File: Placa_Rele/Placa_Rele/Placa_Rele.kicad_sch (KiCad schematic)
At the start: 43 parts, among them J1 Screw_Terminal_Crusher1, J2 MixerScrewTerminal1, J3 FanScrewTerminal1, Q1 2N3904, Q2 2N3904, Q3 2N3904, U1 LM7805_TO220, U2 ESP32-DEVKIT-V1, U3 PC817, U4 PC817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

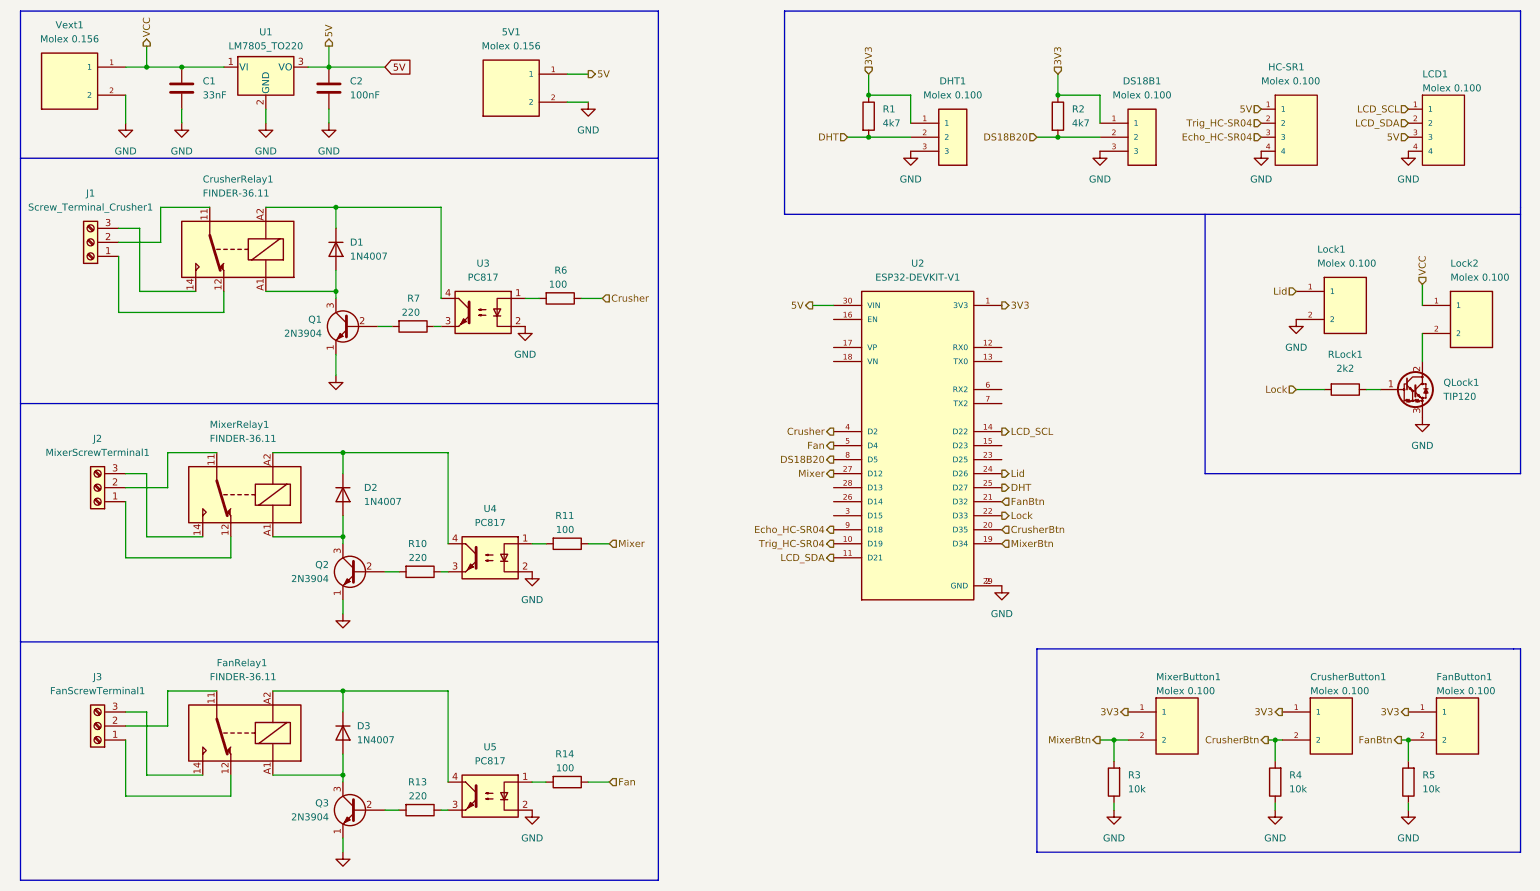
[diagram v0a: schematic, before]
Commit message: Primero Version de PCB con PCB_rele
Primer PCB terminado, los componentes no estan en su posicion final.
El principal problema fue la conexion de 5V, 3v3 y GND en los conectores
del ultrasonico, LCD y DHT.
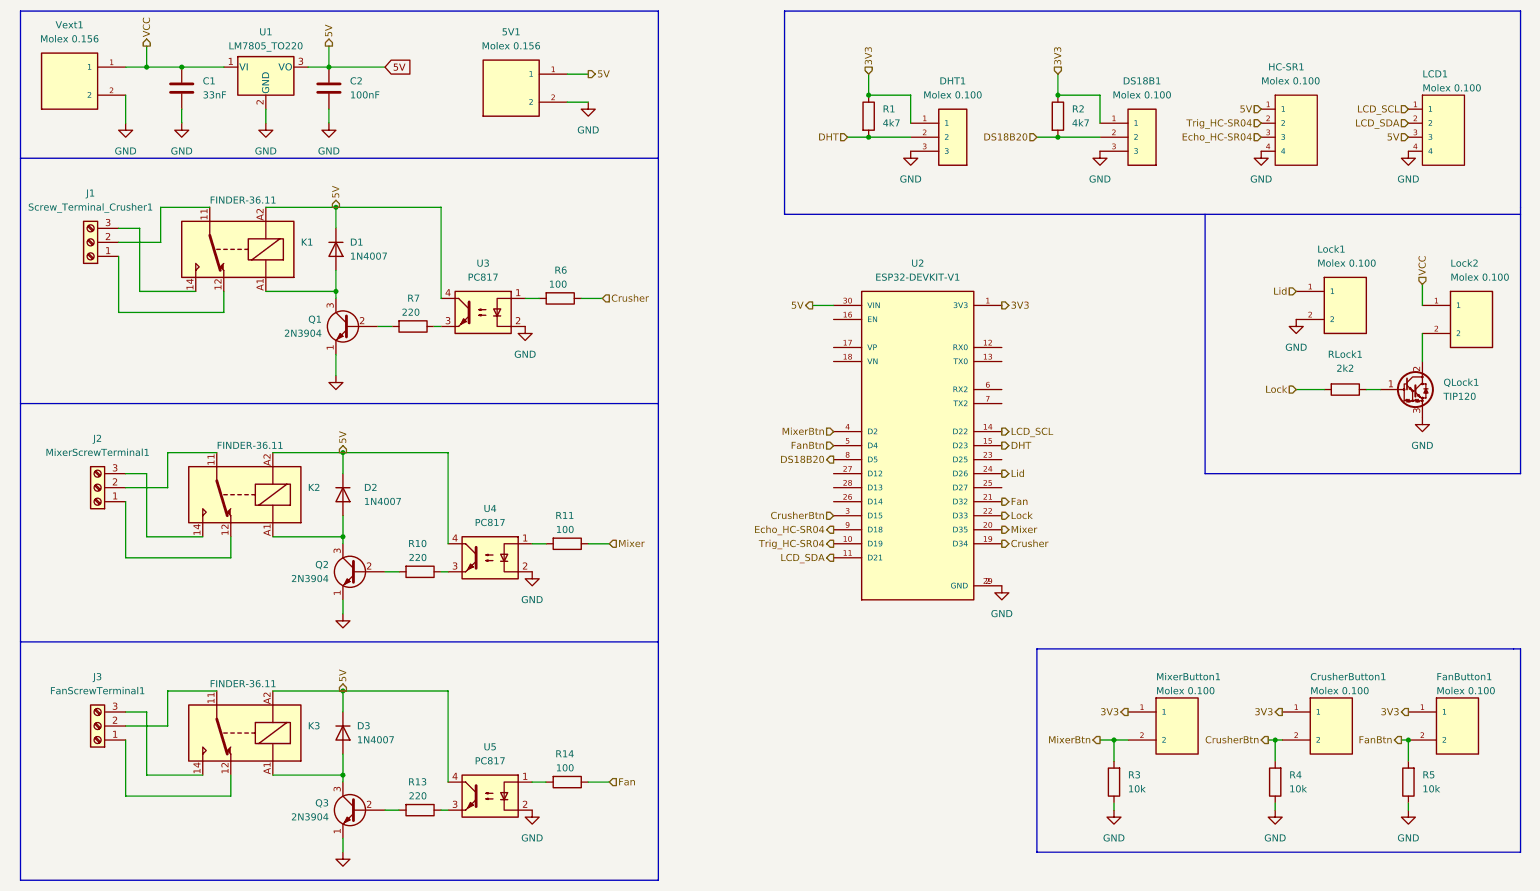
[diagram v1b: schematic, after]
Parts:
- removed CrusherRelay1, FanRelay1, MixerRelay1: FINDER-36.11, Relay_SMD:Relay_DPDT_Kemet_EE2_NU, symbol Relay:FINDER-36.11
- added K1, K2, K3: FINDER-36.11, Relay_THT:Relay_SPDT_Finder_36.11, symbol Relay:FINDER-36.11
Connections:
- net 5V: now also D1.1 (K), D2.1 (K), D3.1 (K), U3.4, U4.4, U5.4, K1.A2, K2.A2, K3.A2
- net Crusher: now also U2.19 (D34); no longer U2.4 (D2)
- net CrusherBtn: now also U2.3 (D15); no longer U2.20 (D35)
- net DHT: now also U2.15 (D23); no longer U2.25 (D27)
- net Fan: now also U2.21 (D32); no longer U2.5 (D4)
- net FanBtn: now also U2.5 (D4); no longer U2.21 (D32)
- net Mixer: now also U2.20 (D35); no longer U2.27 (D12)
- net MixerBtn: now also U2.4 (D2); no longer U2.19 (D34)
- net at J3.2 (Pin_2): now also K3.11
- net at J3.1 (Pin_1): now also K3.12
- net at J3.3 (Pin_3): now also K3.14
- net at D3.2 (A), Q3.3 (C): now also K3.A1
- net at J1.2 (Pin_2): now also K1.11
- net at J1.1 (Pin_1): now also K1.12
- net at J1.3 (Pin_3): now also K1.14
- net at D1.2 (A), Q1.3 (C): now also K1.A1
- net at D2.2 (A), Q2.3 (C): now also K2.A1
- net at J2.2 (Pin_2): now also K2.11
- net at J2.1 (Pin_1): now also K2.12
- net at J2.3 (Pin_3): now also K2.14

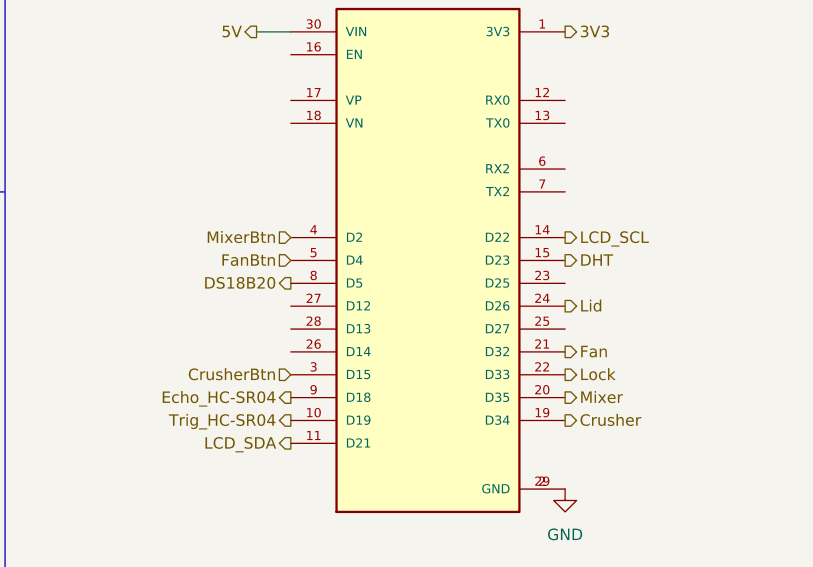
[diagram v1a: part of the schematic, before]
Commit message: Modificacion de PCB
Se cambiaron los ordenes de los GPIO asi DHT y DS18B estaban en los
primeros GPIOS y facilitaba el ruteo.
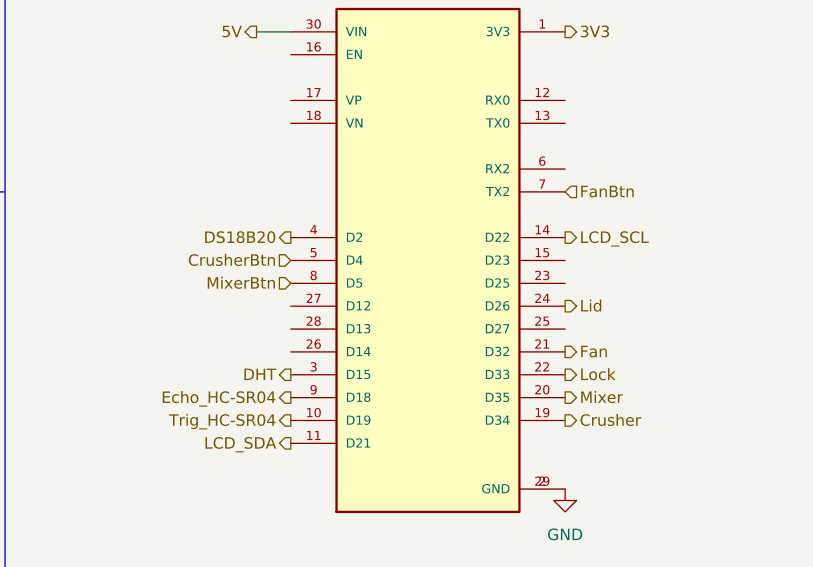
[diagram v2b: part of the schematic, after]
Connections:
- net CrusherBtn: now also U2.5 (D4); no longer U2.3 (D15)
- net DHT: now also U2.3 (D15); no longer U2.15 (D23)
- net DS18B20: now also U2.4 (D2); no longer U2.8 (D5)
- net FanBtn: now also U2.7 (TX2); no longer U2.5 (D4)
- net MixerBtn: now also U2.8 (D5); no longer U2.4 (D2)
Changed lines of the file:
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@@
     (effects (font (size 1.27 1.27)) (justify left))
   )
-  (hierarchical_label "DHT" (shape output) (at 190.5 91.44 0) (fields_autoplaced)
-    (effects (font (size 1.27 1.27)) (justify left))
+  (hierarchical_label "DHT" (shape output) (at 160.02 104.14 180) (fields_autoplaced)
+    (effects (font (size 1.27 1.27)) (justify right))
   )
   (hierarchical_label "Lid" (shape output) (at 190.5 96.52 0) (fields_autoplaced)
@@
     (effects (font (size 1.27 1.27)) (justify right))
   )
-  (hierarchical_label "CrusherBtn" (shape input) (at 160.02 104.14 180) (fields_autoplaced)
+  (hierarchical_label "CrusherBtn" (shape input) (at 160.02 91.44 180) (fields_autoplaced)
     (effects (font (size 1.27 1.27)) (justify right))
   )
@@
     (effects (font (size 1.27 1.27)) (justify right))
   )
-  (hierarchical_label "FanBtn" (shape input) (at 160.02 91.44 180) (fields_autoplaced)
-    (effects (font (size 1.27 1.27)) (justify right))
+  (hierarchical_label "FanBtn" (shape input) (at 190.5 83.82 0) (fields_autoplaced)
+    (effects (font (size 1.27 1.27)) (justify left))
   )
   (hierarchical_label "LCD_SCL" (shape input) (at 264.16 30.48 180) (fields_autoplaced)
@@
     (effects (font (size 1.27 1.27)) (justify left))
   )
-  (hierarchical_label "MixerBtn" (shape input) (at 160.02 88.9 180) (fields_autoplaced)
+  (hierarchical_label "MixerBtn" (shape input) (at 160.02 93.98 180) (fields_autoplaced)
     (effects (font (size 1.27 1.27)) (justify right))
   )
@@
     (effects (font (size 1.27 1.27)) (justify right))
   )
-  (hierarchical_label "DS18B20" (shape output) (at 160.02 93.98 180) (fields_autoplaced)
+  (hierarchical_label "DS18B20" (shape output) (at 160.02 88.9 180) (fields_autoplaced)
     (effects (font (size 1.27 1.27)) (justify right))
   )

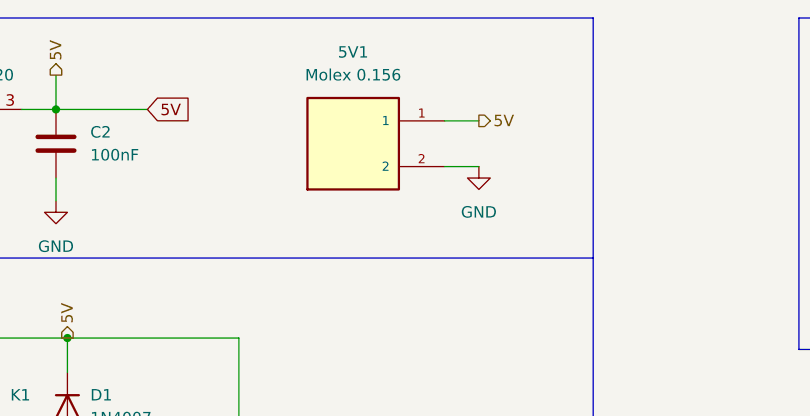
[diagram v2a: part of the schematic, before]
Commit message: Placa final con  reles pero sin LEDS
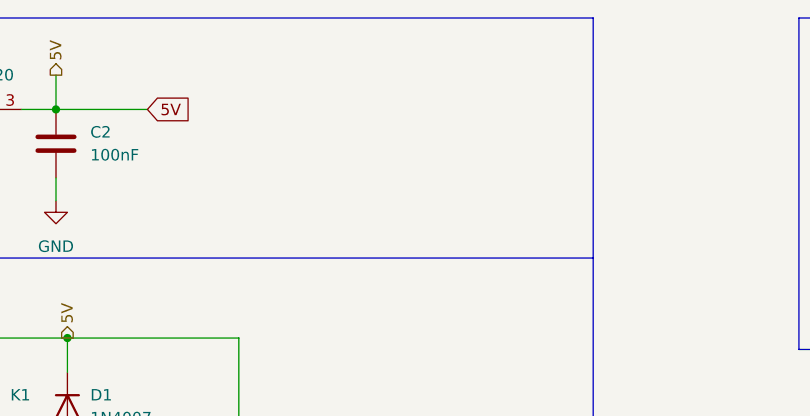
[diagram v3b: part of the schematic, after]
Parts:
- removed 5V1: Molex 0.156, Conectores_Molex:Molex_156_2pines, symbol Conectores_Molex:Molex_156_2pines
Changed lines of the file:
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@@
-    (stroke (width 0) (type default))
-  )
-  (wire (pts (xy 111.76 24.13) (xy 115.57 24.13))
     (stroke (width 0) (type default))
   )
@@
   )
   (wire (pts (xy 71.12 135.89) (xy 90.17 135.89))
-    (stroke (width 0) (type default))
-  )
-  (wire (pts (xy 111.76 29.21) (xy 115.57 29.21))
     (stroke (width 0) (type default))
   )
@@
   )
   (hierarchical_label "Lock" (shape output) (at 190.5 104.14 0) (fields_autoplaced)
-    (effects (font (size 1.27 1.27)) (justify left))
-  )
-  (hierarchical_label "5V" (shape output) (at 115.57 24.13 0) (fields_autoplaced)
     (effects (font (size 1.27 1.27)) (justify left))
   )
@@
         (path "/ced4e9c8-c58e-4967-b7eb-4d589a391933"
           (reference "HC-SR1") (unit 1)
-        )
-      )
-    )
-  )
-  (symbol (lib_id "power:GND") (at 115.57 29.21 0) (unit 1)
-    (in_bom yes) (on_board yes) (dnp no) (fields_autoplaced)
-    (property "Reference" "#PWR08" (at 115.57 35.56 0)
-      (effects (font (size 1.27 1.27)) hide)
-    )
-    (property "Value" "GND" (at 115.57 34.29 0)
-      (effects (font (size 1.27 1.27)))
-    )
-    (property "Footprint" "" (at 115.57 29.21 0)
-      (effects (font (size 1.27 1.27)) hide)
-    )
-    (property "Datasheet" "" (at 115.57 29.21 0)
-      (effects (font (size 1.27 1.27)) hide)
-    )
-    (pin "1")
-    (instances
-      (project "Placa_Rele"
-        (path "/6164fecd-2c83-41e3-903a-21871ef519e8"
-          (reference "#PWR08") (unit 1)
-        )
-      )
-      (project "AutoCompost_Placa"
-        (path "/ced4e9c8-c58e-4967-b7eb-4d589a391933"
-          (reference "#PWR08") (unit 1)
         )
       )
@@
         )
       )
-    )
-  )
-  (symbol (lib_id "Conectores_Molex:Molex_156_2pines") (at 101.6 26.67 0) (unit 1)
-    (in_bom yes) (on_board yes) (dnp no) (fields_autoplaced)
-    (property "Reference" "5V1" (at 101.6 16.51 0)
-      (effects (font (size 1.27 1.27)))
-    )
-    (property "Value" "Molex 0.156" (at 101.6 19.05 0)
-      (effects (font (size 1.27 1.27)))
-    )
-    (property "Footprint" "Conectores_Molex:Molex_156_2pines" (at 101.6 26.67 0)
-      (effects (font (size 1.27 1.27)) (justify bottom) hide)
-    )
-    (property "Datasheet" "" (at 101.6 26.67 0)
-      (effects (font (size 1.27 1.27)) hide)
-    )
-    (property "MF" "Molex" (at 101.6 26.67 0)
-      (effects (font (size 1.27 1.27)) (justify bottom) hide)
-    )
-    (property "Description" "\nConnector Header Through Hole 2 position 0.156 (3.96mm)\n" (at 101.6 26.67 0)
-      (effects (font (size 1.27 1.27)) (justify bottom) hide)
-    )
-    (property "Package" "None" (at 101.6 26.67 0)
-      (effects (font (size 1.27 1.27)) (justify bottom) hide)
-    )
-    (property "Price" "None" (at 101.6 26.67 0)
-      (effects (font (size 1.27 1.27)) (justify bottom) hide)
-    )
-    (property "Check_prices" "https://www.snapeda.com/parts/0026604020/Molex/view-part/?ref=eda" (at 101.6 26.67 0)
-      (effects (font (size 1.27 1.27)) (justify bottom) hide)
-    )
-    (property "STANDARD" "Manufacturer Recommendation" (at 101.6 26.67 0)
-      (effects (font (size 1.27 1.27)) (justify bottom) hide)
-    )
-    (property "PARTREV" "R" (at 101.6 26.67 0)
-      (effects (font (size 1.27 1.27)) (justify bottom) hide)
-    )
-    (property "SnapEDA_Link" "https://www.snapeda.com/parts/0026604020/Molex/view-part/?ref=snap" (at 101.6 26.67 0)
-      (effects (font (size 1.27 1.27)) (justify bottom) hide)
-    )
-    (property "MP" "0026604020" (at 101.6 26.67 0)
-      (effects (font (size 1.27 1.27)) (justify bottom) hide)
-    )
-    (property "Purchase-URL" "https://www.snapeda.com/api/url_track_click_mouser/?unipart_id=702716&manufacturer=Molex&part_name=0026604020&search_term=connector header through hole 2 position 0.156\"" (at 101.6 26.67 0)
-      (effects (font (size 1.27 1.27)) (justify bottom) hide)
-    )
-    (property "Availability" "In Stock" (at 101.6 26.67 0)
-      (effects (font (size 1.27 1.27)) (justify bottom) hide)
-    )
-    (property "MANUFACTURER" "MOLEX" (at 101.6 26.67 0)
-      (effects (font (size 1.27 1.27)) (justify bottom) hide)
-    )
-    (pin "1")
-    (pin "2")
-    (instances
-      (project "Placa_Rele"
-        (path "/6164fecd-2c83-41e3-903a-21871ef519e8"
-          (reference "5V1") (unit 1)
-        )
-      )
-      (project "AutoCompost_Placa"
-        (path "/ced4e9c8-c58e-4967-b7eb-4d589a391933"
-          (reference "5V1") (unit 1)
-        )
-      )
